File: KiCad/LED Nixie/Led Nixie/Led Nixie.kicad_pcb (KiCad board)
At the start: 2 copper layers, 23 x 23 mm, 20 parts

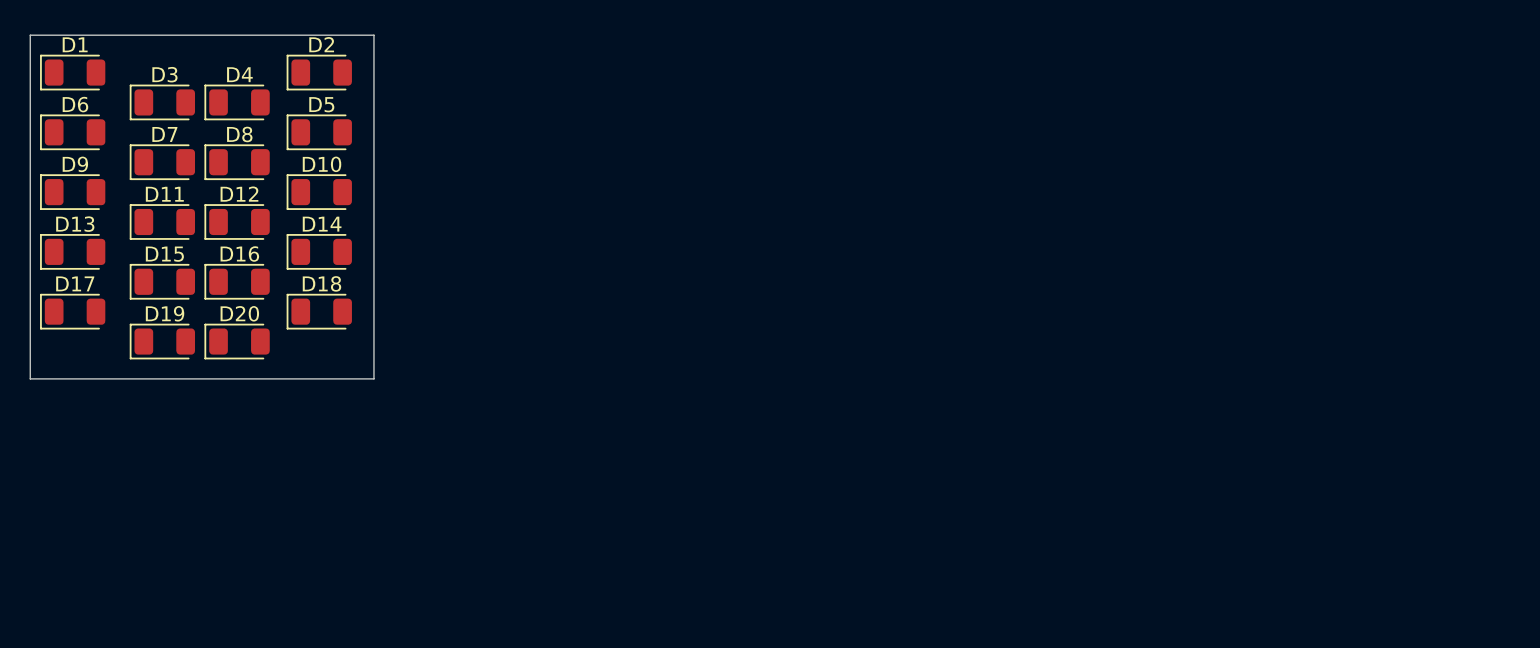
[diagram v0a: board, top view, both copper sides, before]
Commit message: Updated Nixie-PCB
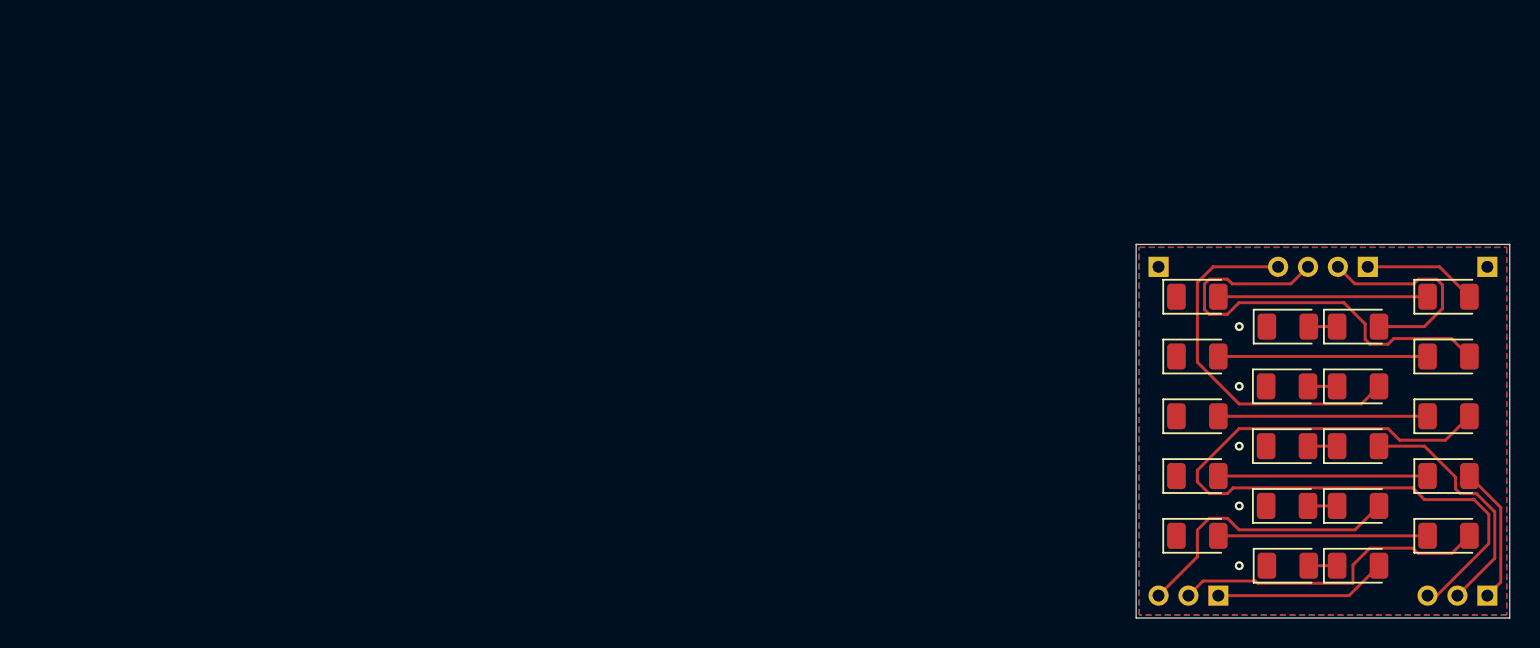
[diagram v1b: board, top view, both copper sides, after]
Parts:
- added J1: Conn_01x04, Connector_PinHeader_2.00mm:PinHeader_1x04_P2.00mm_Vertical, B.Cu at (103.0, 29.0)
- added J2: Conn_01x03, Connector_PinHeader_2.00mm:PinHeader_1x03_P2.00mm_Vertical, B.Cu at (111.0, 51.0)
- added J3: Conn_01x03, Connector_PinHeader_2.00mm:PinHeader_1x03_P2.00mm_Vertical, B.Cu at (93.0, 51.0)
- added J4: Conn_01x01, Connector_PinHeader_2.00mm:PinHeader_1x01_P2.00mm_Vertical, B.Cu at (89.0, 29.0)
- added J5: Conn_01x01, Connector_PinHeader_2.00mm:PinHeader_1x01_P2.00mm_Vertical, B.Cu at (111.0, 29.0)
- D1, D10, D11, D12, D13, D14, D15, D16, D2, D3, D4, D5, D6, D7, D8, D9: footprint LED_SMD:LED_1206_3216Metric -> custom_footprints:LED_1206_3216Metric_nosilkscreen
- D17: renamed from D18; footprint LED_SMD:LED_1206_3216Metric -> custom_footprints:LED_1206_3216Metric_nosilkscreen
- D18: renamed from D17; footprint LED_SMD:LED_1206_3216Metric -> custom_footprints:LED_1206_3216Metric_nosilkscreen
- D19: renamed from D20; footprint LED_SMD:LED_1206_3216Metric -> custom_footprints:LED_1206_3216Metric_nosilkscreen
- D20: renamed from D19; footprint LED_SMD:LED_1206_3216Metric -> custom_footprints:LED_1206_3216Metric_nosilkscreen
- moved D1 93.1 mm to (108.4, 31.0)
- moved D13 93.1 mm to (108.4, 43.0)
- moved D9 93.1 mm to (108.4, 39.0)
- moved D11 81.2 mm to (102.3, 41.0)
- moved D15 81.2 mm to (102.3, 45.0)
- moved D3 81.2 mm to (102.3, 33.0)
- moved D7 81.2 mm to (102.3, 37.0)
- moved D17 76.9 mm to (108.4, 47.0)
- moved D5 76.9 mm to (108.4, 35.0)
- moved D20 76.6 mm to (97.7, 49.0)
- moved D18 76.6 mm to (91.6, 47.0)
- moved D6 76.6 mm to (91.6, 35.0)
- moved D19 76.3 mm to (102.3, 49.0)
- moved D4 71.7 mm to (97.7, 33.0)
- moved D12 71.7 mm to (97.6, 41.0)
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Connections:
- D1 pad 1: unconnected-(D1-K-Pad1) -> Net-(D1-K)
- D1 pad 2: unconnected-(D1-A-Pad2) -> Net-(D1-A)
- D10 pad 1: unconnected-(D10-K-Pad1) -> GND
- D10 pad 2: unconnected-(D10-A-Pad2) -> Net-(D10-A)
- D11 pad 1: unconnected-(D11-K-Pad1) -> Net-(D11-K)
- D11 pad 2: unconnected-(D11-A-Pad2) -> Net-(D11-A)
- D12 pad 1: unconnected-(D12-K-Pad1) -> GND
- D12 pad 2: unconnected-(D12-A-Pad2) -> Net-(D11-K)
- D13 pad 1: unconnected-(D13-K-Pad1) -> Net-(D13-K)
- D13 pad 2: unconnected-(D13-A-Pad2) -> Net-(D13-A)
- D14 pad 1: unconnected-(D14-K-Pad1) -> GND
- D14 pad 2: unconnected-(D14-A-Pad2) -> Net-(D13-K)
- D15 pad 1: unconnected-(D15-K-Pad1) -> Net-(D15-K)
- D15 pad 2: unconnected-(D15-A-Pad2) -> Net-(D15-A)
- D16 pad 1: unconnected-(D16-K-Pad1) -> GND
- D16 pad 2: unconnected-(D16-A-Pad2) -> Net-(D15-K)
- D17 pad 1: unconnected-(D18-K-Pad1) -> Net-(D17-K)
- D17 pad 2: unconnected-(D18-A-Pad2) -> Net-(D17-A)
- D18 pad 1: unconnected-(D17-K-Pad1) -> GND
- D18 pad 2: unconnected-(D17-A-Pad2) -> Net-(D17-K)
- D19 pad 1: unconnected-(D20-K-Pad1) -> Net-(D19-K)
- D19 pad 2: unconnected-(D20-A-Pad2) -> Net-(D19-A)
- D2 pad 1: unconnected-(D2-K-Pad1) -> GND
- D2 pad 2: unconnected-(D2-A-Pad2) -> Net-(D1-K)
- D20 pad 1: unconnected-(D19-K-Pad1) -> GND
- D20 pad 2: unconnected-(D19-A-Pad2) -> Net-(D19-K)
- D3 pad 1: unconnected-(D3-K-Pad1) -> Net-(D3-K)
- D3 pad 2: unconnected-(D3-A-Pad2) -> Net-(D3-A)
- D4 pad 1: unconnected-(D4-K-Pad1) -> GND
- D4 pad 2: unconnected-(D4-A-Pad2) -> Net-(D3-K)
- D5 pad 1: unconnected-(D5-K-Pad1) -> Net-(D5-K)
- D5 pad 2: unconnected-(D5-A-Pad2) -> Net-(D5-A)
- D6 pad 1: unconnected-(D6-K-Pad1) -> GND
- D6 pad 2: unconnected-(D6-A-Pad2) -> Net-(D5-K)
- D7 pad 1: unconnected-(D7-K-Pad1) -> Net-(D7-K)
- D7 pad 2: unconnected-(D7-A-Pad2) -> Net-(D7-A)
- D8 pad 1: unconnected-(D8-K-Pad1) -> GND
- D8 pad 2: unconnected-(D8-A-Pad2) -> Net-(D7-K)
- D9 pad 1: unconnected-(D9-K-Pad1) -> Net-(D10-A)
- D9 pad 2: unconnected-(D9-A-Pad2) -> Net-(D9-A)
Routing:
- net Net-(D9-A): track 0.00 -> 49.3 mm
- net Net-(D5-A): track 0.00 -> 30.0 mm
- net Net-(D7-A): track 0.00 -> 25.0 mm
- net Net-(D17-A): track 0.00 -> 21.6 mm
- net Net-(D15-A): track 0.00 -> 18.9 mm
- net Net-(D11-A): track 0.00 -> 16.7 mm
- net Net-(D3-A): track 0.00 -> 14.1 mm
- net Net-(D5-K): track 0.00 -> 14.0 mm
- net Net-(D17-K): track 0.00 -> 14.0 mm
- net Net-(D13-K): track 0.00 -> 14.0 mm
- net Net-(D10-A): track 0.00 -> 14.0 mm
- net Net-(D1-K): track 0.00 -> 14.0 mm
- net Net-(D19-A): track 0.00 -> 11.6 mm
- net Net-(D13-A): track 0.00 -> 9.24 mm
- net Net-(D1-A): track 0.00 -> 7.63 mm
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- added copper zone on B.Cu, net GND
- added copper zone on F.Cu, net GND
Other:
- board size 23 x 23 mm -> 25 x 25 mm
- board text added: "JLCJLCJLC"
- board text added: "LED-Nixie"
- board text added: "Rev.A - 06/24"
- board text added: "github.com/d3molite/LED-Nixie"

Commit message: updated PCB
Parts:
- moved J1 6.10 mm to (96.9, 29.0), turned to -90 degrees
- moved J2 4.00 mm to (107.0, 51.0), turned to -90 degrees
- moved J3 4.00 mm to (89.0, 51.0), turned to -90 degrees
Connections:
- J2 pad 1: Net-(D13-A) -> Net-(D9-A)
- J2 pad 3: Net-(D9-A) -> Net-(D13-A)
- J3 pad 1: Net-(D19-A) -> Net-(D15-A)
- J3 pad 3: Net-(D15-A) -> Net-(D19-A)
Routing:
- net Net-(D5-A): track 30.0 -> 64.0 mm
- net Net-(D1-A): track 7.63 -> 40.4 mm
- net Net-(D7-A): track 25.0 -> 40.1 mm
- net Net-(D3-A): track 14.1 -> 24.2 mm
- net GND: track 0.00 -> 9.10 mm
